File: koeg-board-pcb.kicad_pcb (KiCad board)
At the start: 2 copper layers, 228.3 x 84.3 mm, 226 parts, among them J1 Conn_01x02, J2 SWD_Connector, J3 USB_C_Receptacle_USB2.0_14P, J4 Conn_01x02, J5 SWD_Connector, J6 USB_C_Receptacle_USB2.0_14P, Q1 BSS138, Q2 BSS138, SW1 Reset Button, SW10 SW_Push, SW11 SW_Push, SW12 SW_Push, SW13 SW_Push, SW14 SW_Push, SW15 SW_Push, SW16 SW_Push, SW17 SW_Push, SW18 SW_Push, SW19 SW_Push, SW2 SW_On_Off, SW20 SW_Push, SW21 SW_Push, SW22 SW_Push, SW23 SW_Push, SW24 Reset Button, SW25 SW_On_Off, SW26 SW_Push, SW27 SW_Push, SW28 SW_Push, SW29 SW_Push, SW3 SW_Push, SW30 SW_Push, SW31 SW_Push, SW32 SW_Push, SW33 SW_Push, SW34 SW_Push, SW35 SW_Push, SW36 SW_Push, SW37 SW_Push, SW38 SW_Push, SW39 SW_Push, SW4 SW_Push, SW40 SW_Push, SW41 SW_Push, SW42 SW_Push, SW43 SW_Push, SW44 SW_Push, SW45 SW_Push, SW46 SW_Push, SW5 SW_Push, SW6 SW_Push, SW7 SW_Push, SW8 SW_Push, SW9 SW_Push, U2 USBLC6-2SC6, U4 TPS61252DSG, U5 USBLC6-2SC6, U6 TPS61252DSG, U7 nRF52833_QDxx, U8 nRF52833_QDxx, Y1 JYJE 2TJ432000NYFBC, Y2 JYJE 2TJ432000NYFBC, Y3 32.768 kHz, Y4 32.768 kHz

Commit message: placed components
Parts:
- added C15: 12pF, Capacitor_SMD:C_0402_1005Metric, B.Cu at (252.1, 118.0)
- added C16: 12pF, Capacitor_SMD:C_0402_1005Metric, B.Cu at (46.8, 120.3)
- added C31: 12pF, Capacitor_SMD:C_0402_1005Metric, B.Cu at (251.1, 118.0)
- added C32: 12pF, Capacitor_SMD:C_0402_1005Metric, B.Cu at (45.8, 120.3)
- AE2: moved to F.Cu
- C1, C13, C14, C17, C18, C19, C29, C3, C30, D1, D22, D43, L1, L10, L2, L3, L4, L5, L6, L7, L8, L9, Q1, Q2, R10, R13, R14, R15, R16, R17, R18, R2, R3, R6, R7, R8, R9, U2, U5, U6, U7, U8, Y3, Y4: moved to B.Cu
- C10, C11, C12, C20, C21, C22, C23, C24, C25, C26, C27, C28, C4, C5, C6, C7, C8, C9: footprint Capacitor_SMD:C_0603_1608Metric -> Capacitor_SMD:C_0402_1005Metric; moved to B.Cu
- C33, C34, C35, C36, C37, C38: footprint Capacitor_SMD:C_0603_1608Metric -> Capacitor_SMD:C_0805_2012Metric; moved to B.Cu
- Y1, Y2: value JYJE 2TJ432000NYFBC -> 32MHz; moved to B.Cu
- moved U6 330.5 mm to (35.4, 104.3)
- moved Q2 328.5 mm to (36.3, 127.2), turned to 180 degrees
- moved R14 327.2 mm to (33.7, 126.8), turned to -90 degrees
- moved R13 324.9 mm to (36.0, 129.5)
- moved L8 324.3 mm to (37.5, 103.7), turned to 90 degrees
- moved R9 316.3 mm to (38.7, 117.5), turned to -90 degrees
- moved R10 315.5 mm to (39.7, 117.5), turned to 90 degrees
- moved L7 315.4 mm to (38.8, 126.8), turned to -90 degrees
- moved Y2 315.3 mm to (39.9, 131.4), turned to 90 degrees
- moved L6 309.7 mm to (40.0, 123.6), turned to 90 degrees
- moved C27 309.1 mm to (37.9, 131.4), turned to 90 degrees
- moved C28 309.0 mm to (41.9, 132.2), turned to -90 degrees
- moved L9 308.8 mm to (45.4, 130.8), turned to -90 degrees
- moved L10 307.6 mm to (46.5, 131.4)
- moved C26 307.1 mm to (39.9, 129.1), turned to 180 degrees
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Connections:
- net /left/DEC4 renamed /left/DEC4-6
- net /right/DEC4 renamed /right/DEC4-6
- U7 pad 23: /left/COL0 -> unconnected-(U7-NFC2/P0.10-Pad23)
- U7 pad 33: unconnected-(U7-AIN4/P0.28-Pad33) -> /left/LED_PIN
- U7 pad 34: unconnected-(U7-AIN5/P0.29-Pad34) -> /left/COL0
- U7 pad 36: /left/LED_PIN -> unconnected-(U7-AIN7/P0.31-Pad36)
- U8 pad 23: /right/COL0 -> unconnected-(U8-NFC2/P0.10-Pad23)
- U8 pad 33: unconnected-(U8-AIN4/P0.28-Pad33) -> /right/LED_PIN
- U8 pad 34: unconnected-(U8-AIN5/P0.29-Pad34) -> /right/COL0
- U8 pad 36: /right/LED_PIN -> unconnected-(U8-AIN7/P0.31-Pad36)
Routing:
- added copper zone on In1.Cu, net /left/leds/LED_5V
- added copper zone on In2.Cu, net GND
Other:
- copper layers 2 -> 4

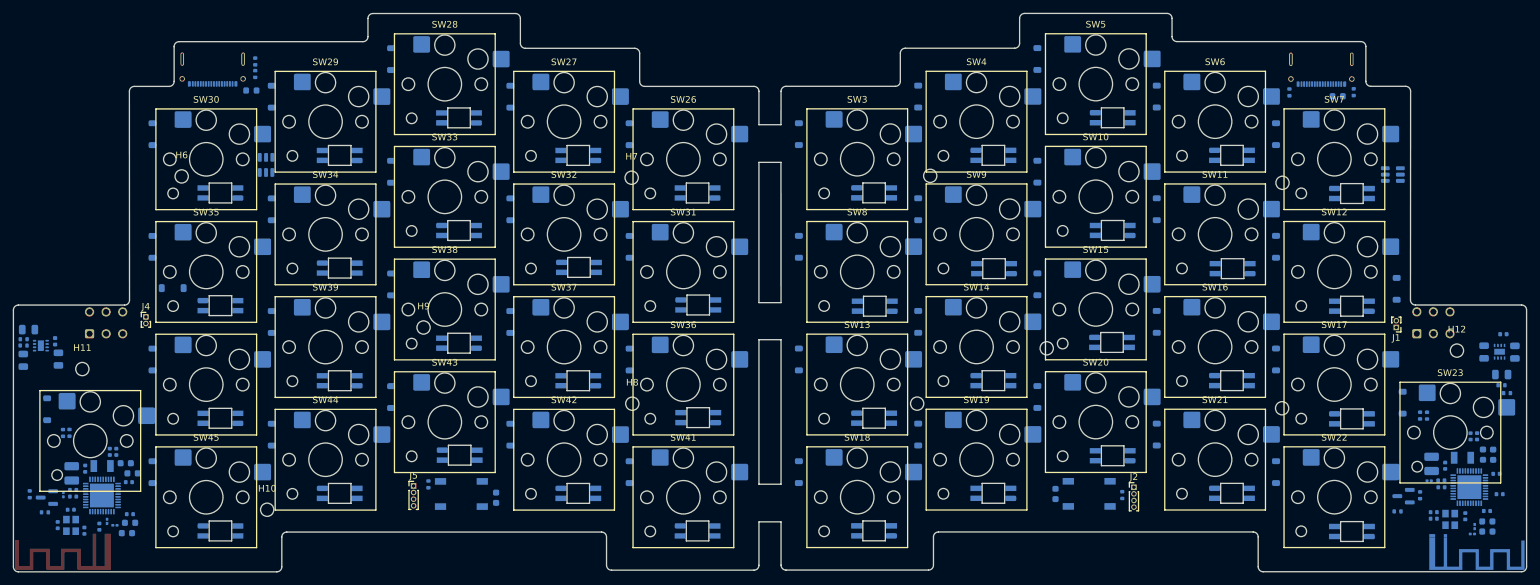
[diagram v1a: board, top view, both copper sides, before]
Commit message: the right side still needs to be routed
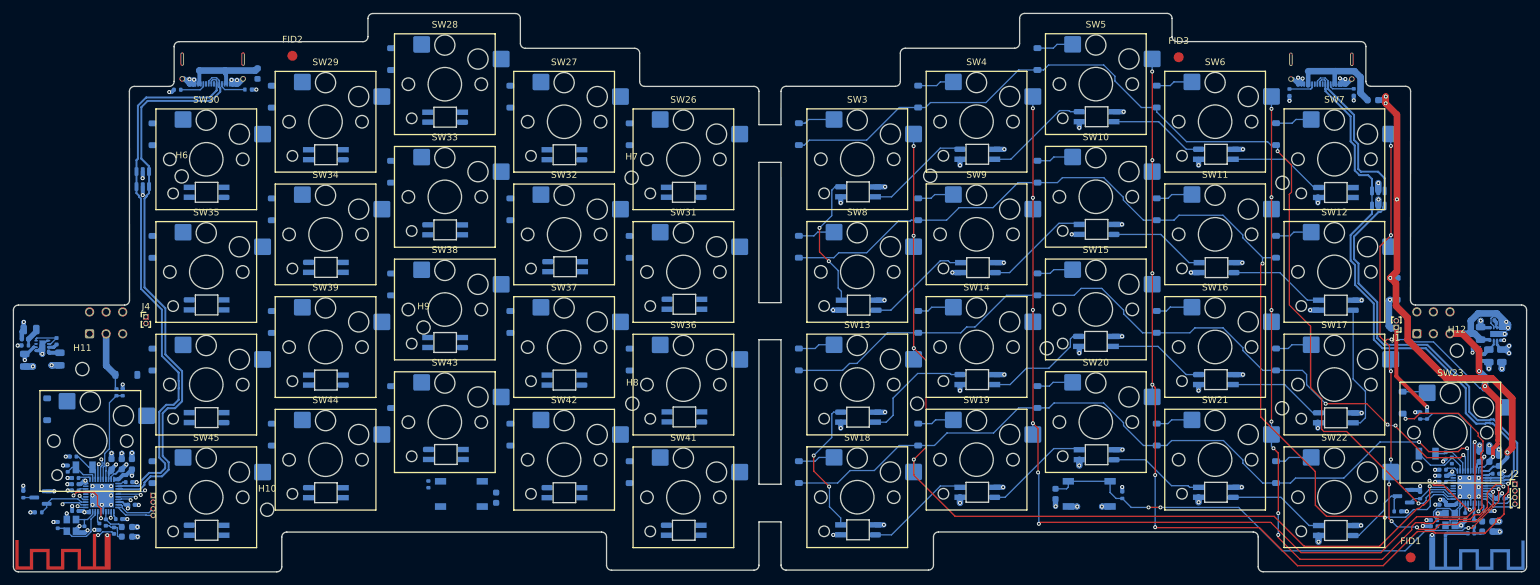
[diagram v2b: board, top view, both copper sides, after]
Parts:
- removed C24, C8: 47nF, Capacitor_SMD:C_0402_1005Metric
- removed L1, L6: 10uH, Inductor_SMD:L_1008_2520Metric
- removed L2, L7: 15nH, Inductor_SMD:L_0201_0603Metric
- added C39: 1uF, Capacitor_SMD:C_0402_1005Metric, B.Cu at (246.9, 124.0)
- added C40: 1uF, Capacitor_SMD:C_0402_1005Metric, B.Cu at (40.6, 125.2)
- added C41: 100nF, Capacitor_SMD:C_0402_1005Metric, B.Cu at (246.9, 128.3)
- added C42: 100nF, Capacitor_SMD:C_0402_1005Metric, B.Cu at (40.6, 129.3)
- added C43: 100nF, Capacitor_SMD:C_0402_1005Metric, B.Cu at (255.7, 127.4)
- added C44: 100nF, Capacitor_SMD:C_0402_1005Metric, B.Cu at (49.0, 128.3)
- added FID1: Fiducial, Fiducial:Fiducial_1.5mm_Mask3mm, F.Cu at (242.1, 136.3)
- added FID2: Fiducial, Fiducial:Fiducial_1.5mm_Mask3mm, F.Cu at (73.3, 60.6)
- added FID3: Fiducial, Fiducial:Fiducial_1.5mm_Mask3mm, F.Cu at (207.1, 60.8)
- C10, C26: footprint Capacitor_SMD:C_0402_1005Metric -> Capacitor_SMD:C_0603_1608Metric
- J3, J6: value USB_C_Receptacle_USB2.0_14P -> USB_C_Receptacle_USB2.0_16P
- J5: moved to B.Cu
- L10, L4, L5, L9: footprint Inductor_SMD:L_0201_0603Metric -> Inductor_SMD:L_0402_1005Metric
- moved J2 57.5 mm to (257.8, 125.2)
- moved J5 39.3 mm to (52.3, 126.9), turned to 180 degrees
- moved U5 18.7 mm to (50.7, 79.2)
- moved D43 14.8 mm to (48.3, 108.7)
- moved R11 12.5 mm to (56.0, 65.7), turned to 180 degrees
- moved R9 10.1 mm to (46.8, 111.4)
- moved R10 10.1 mm to (47.7, 111.4)
- moved C26 9.21 mm to (46.0, 122.2), turned to -90 degrees
- moved R17 8.26 mm to (251.9, 104.7), turned to 180 degrees
- moved C32 6.84 mm to (39.4, 122.9)
- moved C16 6.55 mm to (40.2, 121.1), turned to 0 degrees
- moved C10 6.40 mm to (252.5, 121.1), turned to -90 degrees
- moved C15 5.55 mm to (247.4, 120.9), turned to 90 degrees
- moved R15 5.38 mm to (252.4, 106.1), turned to 90 degrees
- moved Y3 5.36 mm to (244.6, 120.6)
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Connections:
- net /left/D+ renamed /left/USB_D+
- net /left/D- renamed /left/USB_D-
- net /right/D+ renamed /right/USB_D+
- net /right/D- renamed /right/USB_D-
- C10 pad 1: /left/V_SYS -> GND
- C10 pad 2: GND -> /left/V_SYS
- C26 pad 1: /right/V_SYS -> GND
- C26 pad 2: GND -> /right/V_SYS
- J3 pad A8: (no net) -> unconnected-(J3-SBU1-PadA8)
- J3 pad B8: (no net) -> unconnected-(J3-SBU2-PadB8)
- J3 pad GND: (no net) -> GND
- J6 pad A8: (no net) -> unconnected-(J6-SBU1-PadA8)
- J6 pad B8: (no net) -> unconnected-(J6-SBU2-PadB8)
- J6 pad GND: (no net) -> GND
- U7 pad 39: /left/DCC -> unconnected-(U7-DCC-Pad39)
- U8 pad 39: /right/DCC -> unconnected-(U8-DCC-Pad39)
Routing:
- net /left/COL1: track 0.00 -> 155.2 mm, vias 0 -> 7
- net /left/ROW0: track 0.00 -> 154.6 mm, vias 0 -> 2
- net /left/COL0: track 0.00 -> 149.3 mm, vias 0 -> 5
- net /left/ROW1: track 0.00 -> 148.0 mm, vias 0 -> 2
- net /left/COL2: track 0.00 -> 143.1 mm, vias 0 -> 7
- net /left/ROW2: track 0.00 -> 120.8 mm, vias 0 -> 4
- net /left/ROW3: track 0.00 -> 118.8 mm, vias 0 -> 2
- net /left/COL3: track 0.00 -> 115.2 mm, vias 0 -> 8
- net /left/COL4: track 0.00 -> 106.8 mm, vias 0 -> 9
- net GND: track 0.00 -> 104.9 mm, vias 0 -> 101
- net /left/USB_D+: track 0.00 -> 89.6 mm
- net /right/USB_D+: track 0.00 -> 86.2 mm
- net /left/USB_D-: track 0.00 -> 85.7 mm
- net /right/USB_D-: track 0.00 -> 83.9 mm
- net /left/RESET: track 0.00 -> 80.2 mm, vias 0 -> 4
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- added copper zone on In1.Cu, net /right/leds/LED_5V

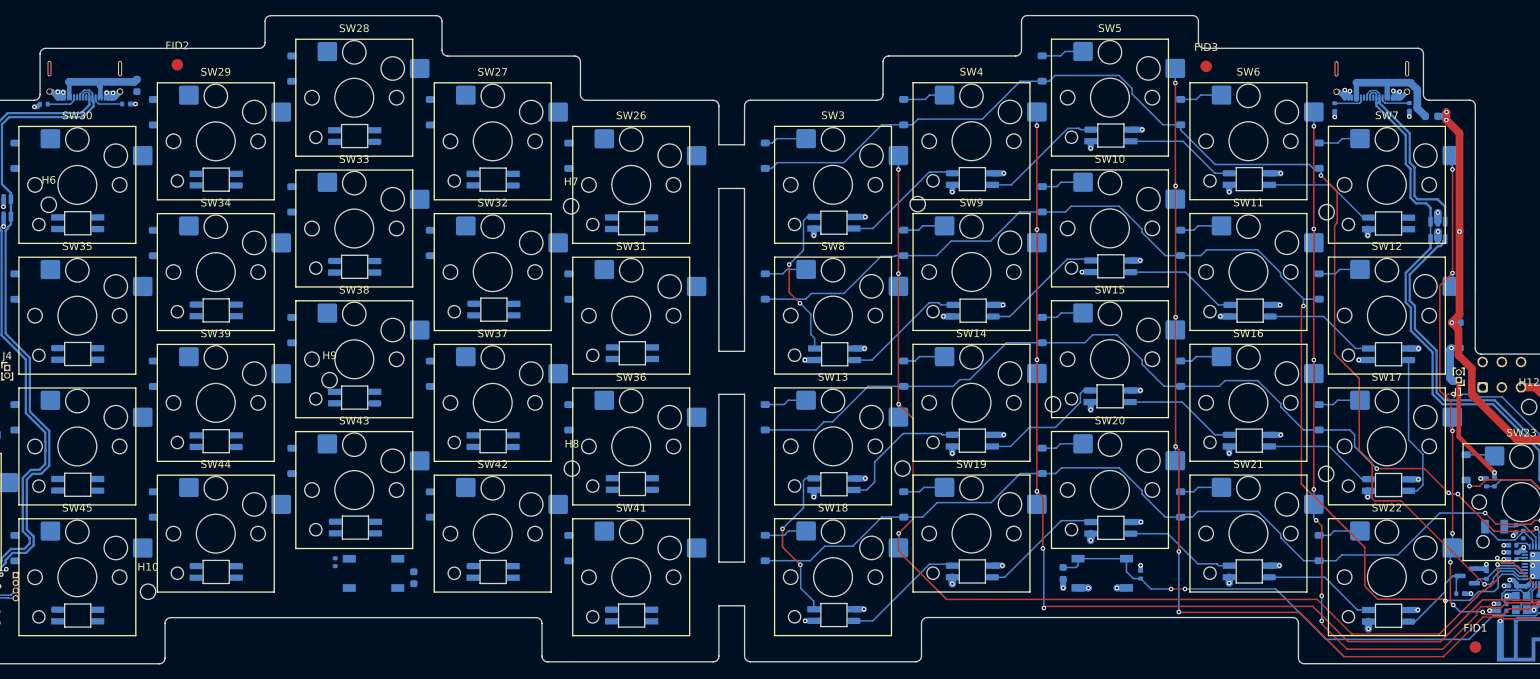
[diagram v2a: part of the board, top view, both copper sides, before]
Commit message: chaned usb c footprint, flipped fiducials
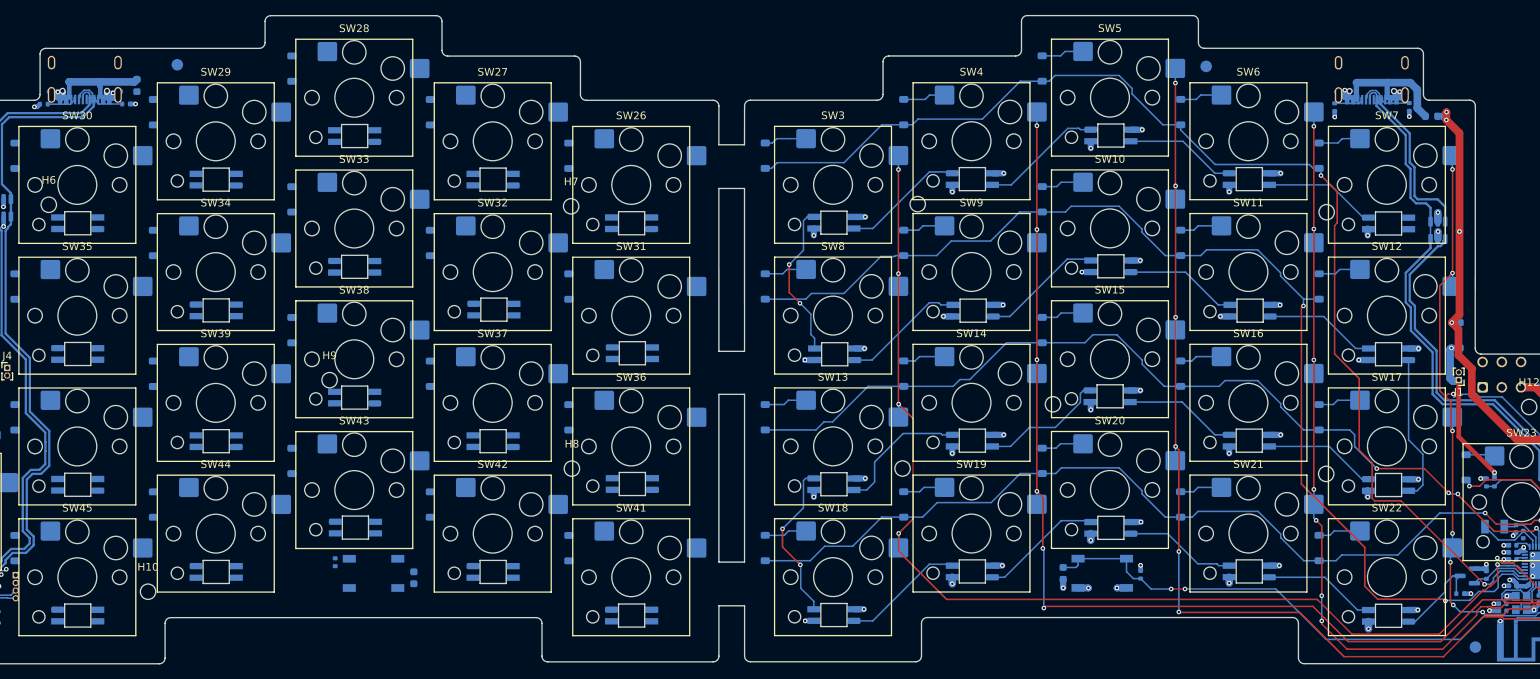
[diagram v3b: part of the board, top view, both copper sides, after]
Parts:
- FID1, FID2, FID3: moved to B.Cu
- J3, J6: footprint Connector_USB:USB_C_Receptacle_G-Switch_GT-USB-7025 -> Connector_USB:USB_C_Receptacle_G-Switch_GT-USB-7010ASV
- turned FID1 to 180 degrees
- turned FID2 to 180 degrees
- turned FID3 to 180 degrees

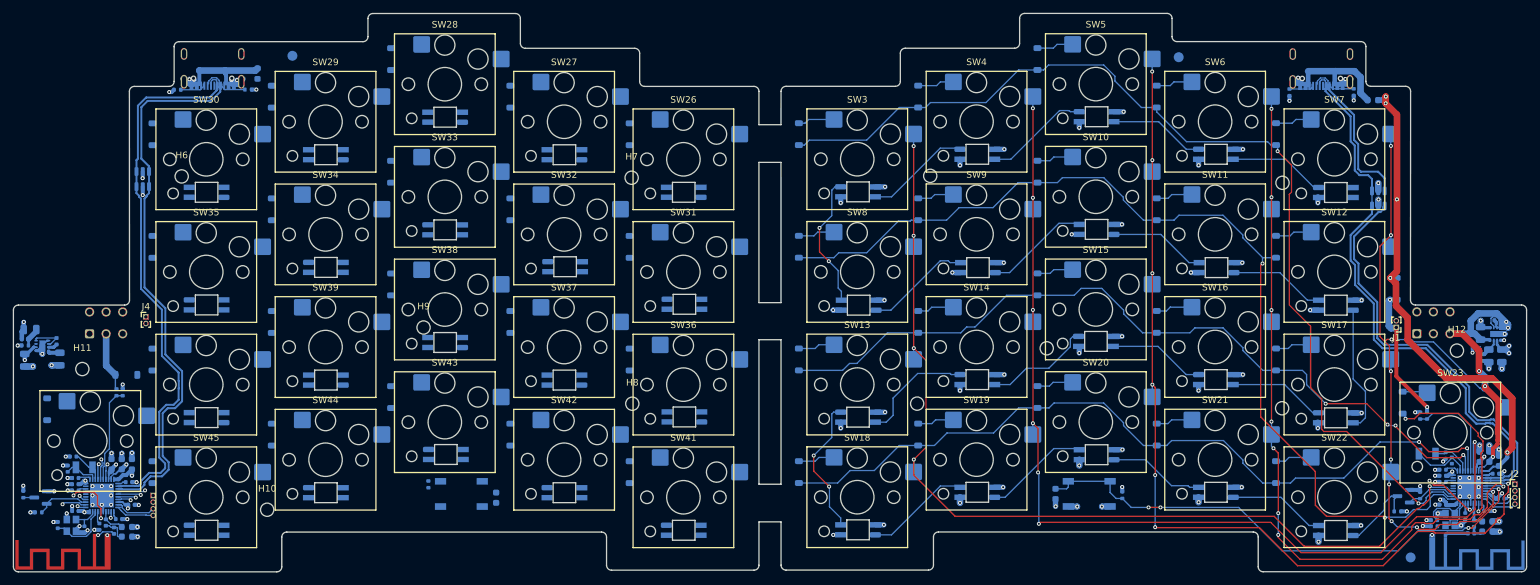
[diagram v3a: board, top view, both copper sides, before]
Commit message: adding power and battery management
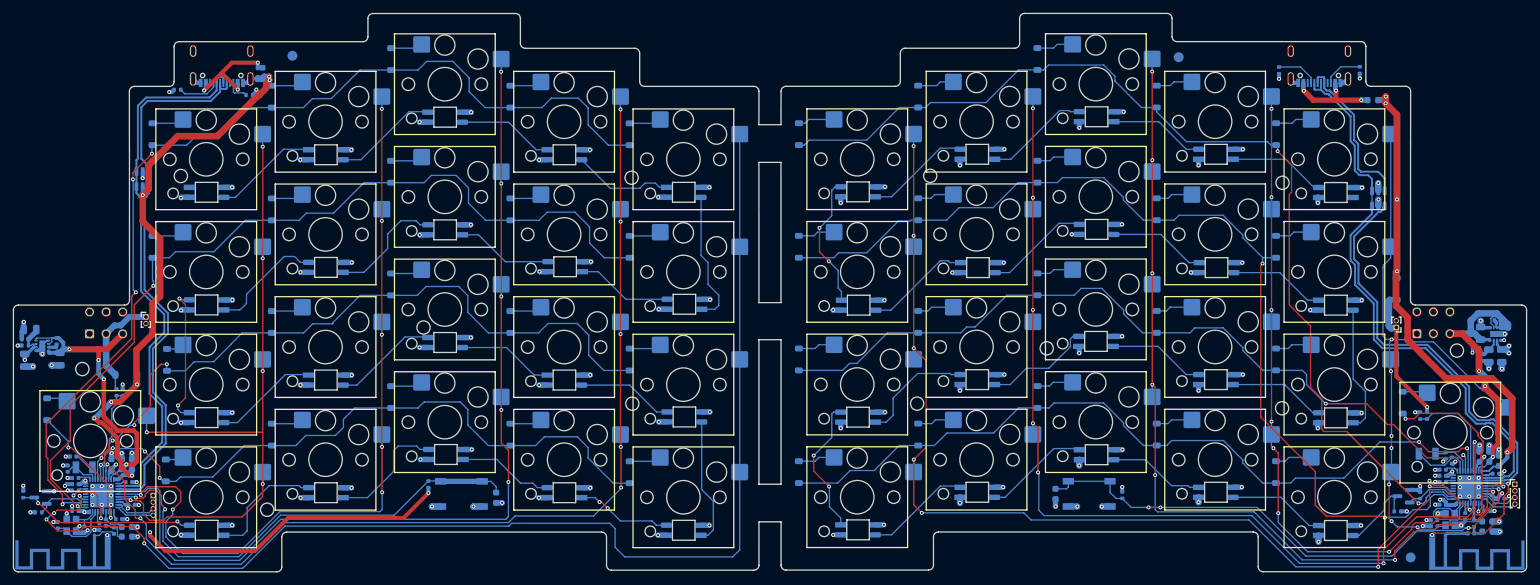
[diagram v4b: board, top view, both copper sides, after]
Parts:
- AE2: footprint pcb_ant:pcb_antenna -> pcb_ant:flipped_pcb_antenna; moved to B.Cu
- moved R4 3.67 mm to (222.2, 62.8)
- moved R5 3.44 mm to (234.4, 62.8)
- moved D58 2.18 mm to (54.4, 106.5)
- moved D63 2.02 mm to (54.2, 123.2)
- moved J6 1.44 mm to (62.7, 61.0)
- moved R12 0.84 mm to (66.8, 66.5)
- moved F2 0.73 mm to (68.8, 63.2)
- moved J3 0.54 mm to (228.3, 61.0)
- moved H6 0.13 mm to (56.5, 78.7)
- turned AE2 to 0 degrees
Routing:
- net /right/COL0: track 1.18 -> 187.4 mm, vias 1 -> 4
- net /right/COL1: track 2.36 -> 159.2 mm, vias 1 -> 7
- net /right/ROW0: track 3.73 -> 152.3 mm, vias 1 -> 4
- net /right/COL2: track 4.16 -> 146.3 mm, vias 1 -> 5
- net /right/ROW1: track 1.31 -> 133.1 mm, vias 1 -> 2
- net /right/COL3: track 3.47 -> 122.5 mm, vias 1 -> 7
- net /right/ROW2: track 2.34 -> 108.7 mm, vias 1 -> 4
- net /right/COL4: track 2.00 -> 105.6 mm, vias 1 -> 6
- net /right/ROW3: track 3.17 -> 101.0 mm, vias 1 -> 4
- net /right/5V: track 5.44 -> 90.9 mm, vias 2 -> 7
- net /right/RESET: track 2.72 -> 72.1 mm, vias 1 -> 2
- net /right/V_SYS: track 10.2 -> 63.5 mm, vias 6 -> 8
- net /left/V_SYS: track 44.0 -> 94.9 mm
- net /right/3.2V-5V: track 10.4 -> 46.2 mm, vias 1 -> 4
- net /right/leds/DATA: track 1.66 -> 27.1 mm, vias 0 -> 2
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- added copper zone on In1.Cu, net /right/V_SYS
